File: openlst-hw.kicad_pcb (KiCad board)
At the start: 4 copper layers, 60 x 50 mm, 175 parts, among them J1 5VDC, J2 CC Prog/Debug, J3 UART0, J4 UART1, J5 Control Outputs, J6 ANT, U1 LM1117-3.3, U2 CC1110, U3 LT1086-3.6, U4 FOX924 27MHz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

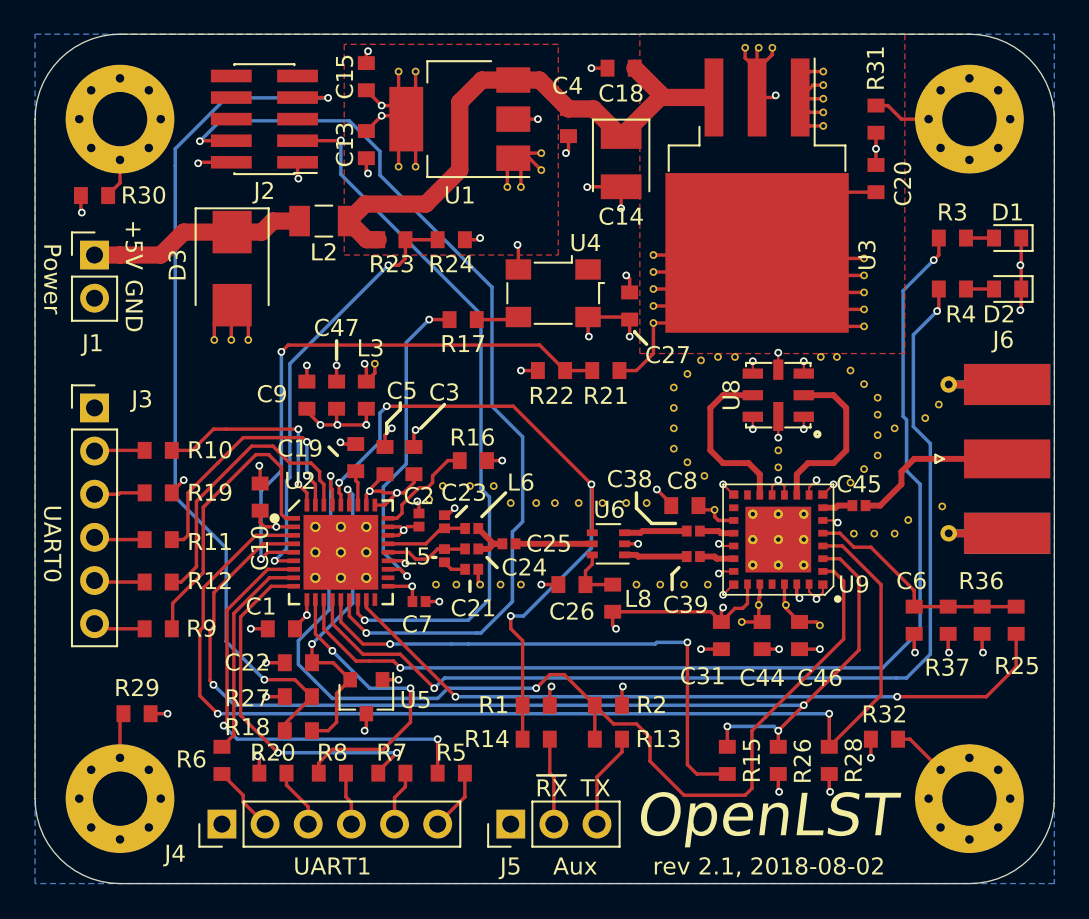
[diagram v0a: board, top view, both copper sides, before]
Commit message: Migrate to KiCad 7 files, schematic visual cleanup, pcb routing cleanup
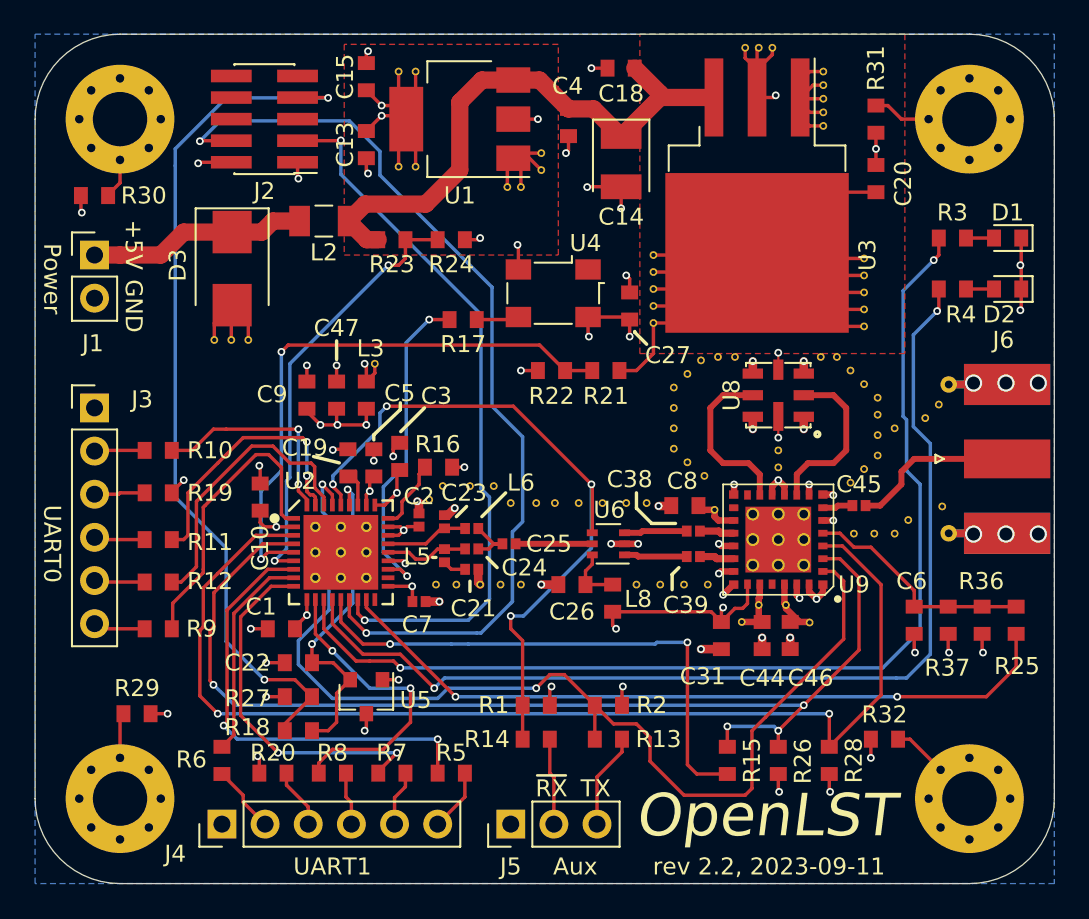
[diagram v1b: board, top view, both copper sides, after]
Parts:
- moved R16 2.09 mm to (137.2, 64.0)
- moved C3 0.87 mm to (135.0, 63.4)
- moved C5 0.67 mm to (133.4, 63.7)
- moved REF** 0.63 mm to (159.1, 73.1)
- moved C19 0.55 mm to (131.9, 63.7)
- moved C46 0.55 mm to (157.9, 73.9)
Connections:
- net /~LST_RESET renamed /~{LST_RESET}
- net /~LST_RX_MODE renamed /~{LST_RX_MODE}
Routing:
- net GND: track 94.4 -> 91.8 mm, vias 56 -> 63
- net /3V3_FILT: track 24.4 -> 22.0 mm
- net Net-(R16-Pad2): track 6.16 -> 4.21 mm
- net /LST_TX_MODE: track 63.9 -> 63.3 mm
- net VCC_3V6: track 105.7 -> 105.1 mm
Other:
- net class 50ohm removed
- net class 8mil removed
- net class Default removed
- net class PWR removed
- board text added: "rev 2.2, 2023-09-11"
- board text added: "rwk brb"
- board text added: "~{RX}"
- board text removed: "rev 2.1, 2018-08-02"
- board text removed: "rwk"
- board text removed: "~RX"

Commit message: DRC cleanup
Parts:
- moved C19 0.13 mm to (131.9, 63.6)
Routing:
- net /LST_TX_MODE: track 63.3 -> 64.5 mm

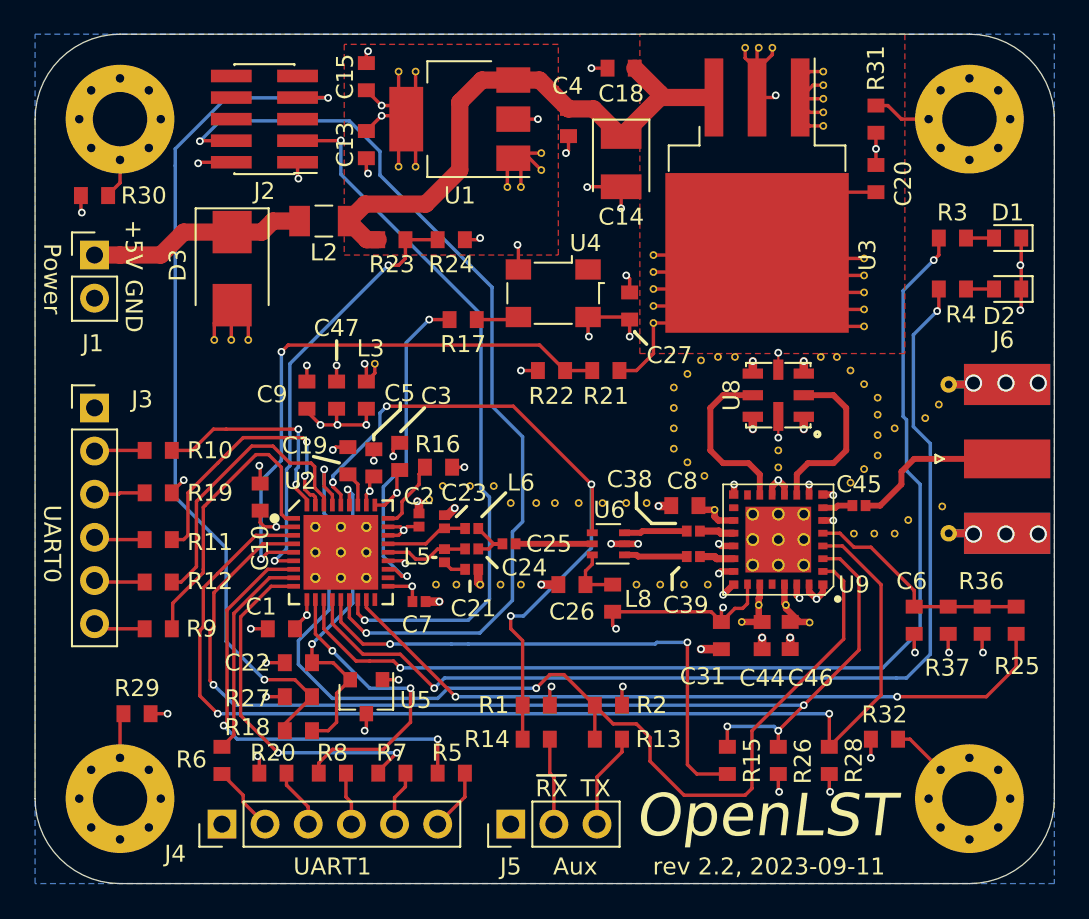
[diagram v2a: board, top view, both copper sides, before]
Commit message: Replace stitching pads with vias, add top ground fill
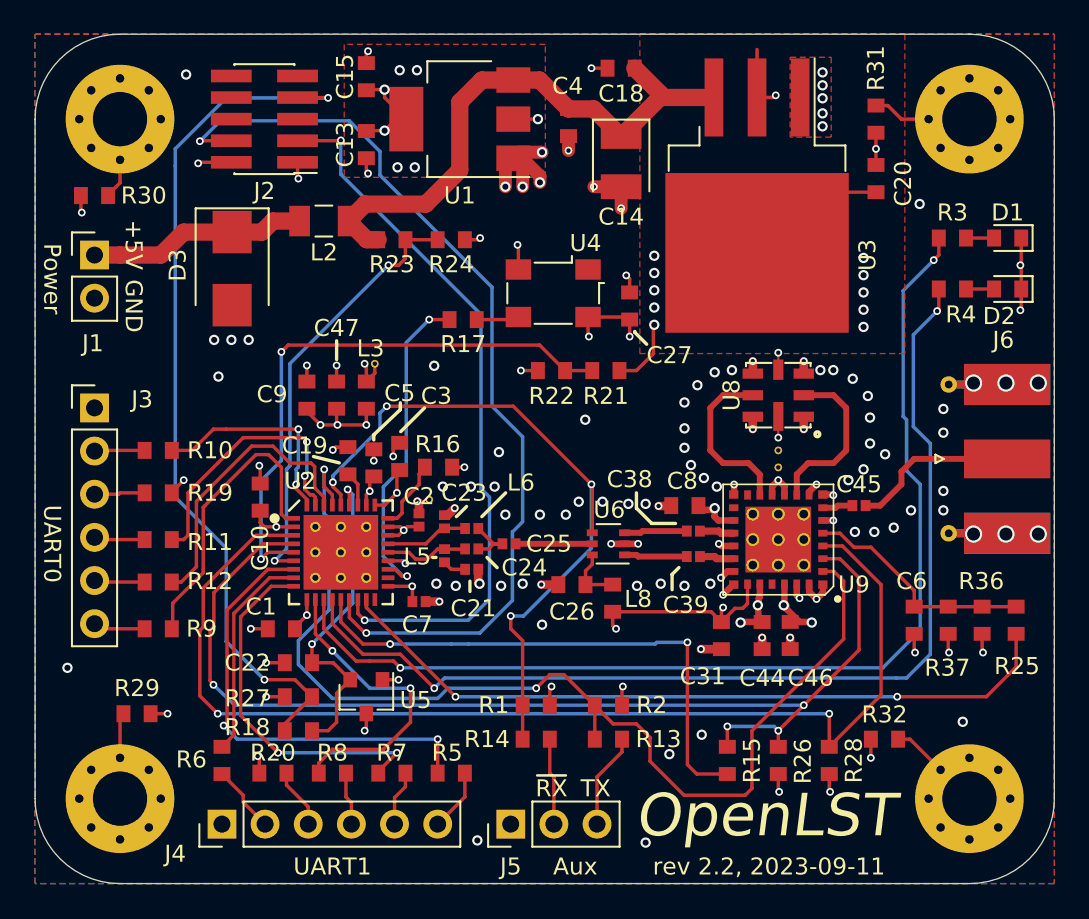
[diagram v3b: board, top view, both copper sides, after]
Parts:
- removed the REF** at (137.1, 70.9)
- removed the REF** at (153.7, 57.5)
- removed the REF** at (161.5, 64.9)
- removed the REF** at (163.1, 62.1)
- removed the REF** at (163.1, 60.9)
- removed the REF** at (163.1, 59.9)
- removed the REF** at (159.8, 57.5)
- removed the REF** at (164.1, 61.7)
- removed the REF** at (161.7, 67.9)
- removed the REF** at (162.9, 67.9)
- removed the REF** at (164.9, 67.1)
- removed the REF** at (166.9, 66.3)
- removed the REF** at (162.3, 64.1)
- removed the REF** at (160.7, 57.5)
- removed the REF** at (151.1, 59.3)
- removed the REF** at (149.5, 66.1)
- removed the REF** at (148.3, 66.1)
- removed the REF** at (146.9, 66.1)
- removed the REF** at (145.5, 66.1)
- removed the REF** at (144.1, 66.1)
- removed the REF** at (152.9, 64.5)
- removed the REF** at (143.0, 66.1)
- removed the REF** at (141.5, 66.1)
- removed the REF** at (140.5, 65.1)
- removed the REF** at (139.1, 65.1)
- removed the REF** at (137.5, 65.1)
- removed the REF** at (153.1, 70.9)
- removed the REF** at (151.7, 70.9)
- removed the REF** at (150.3, 70.9)
- removed the REF** at (148.9, 70.9)
- removed the REF** at (151.9, 63.7)
- removed the REF** at (142.1, 70.9)
- removed the REF** at (140.9, 70.9)
- removed the REF** at (139.7, 70.9)
- removed the REF** at (138.3, 70.9)
- removed the REF** at (151.1, 62.9)
- removed the REF** at (151.9, 58.5)
- removed the REF** at (154.7, 57.5)
- removed the REF** at (162.3, 59.1)
- removed the REF** at (163.1, 63.3)
- removed the REF** at (165.9, 61.1)
- removed the REF** at (151.1, 61.7)
- removed the REF** at (164.1, 67.9)
- removed the REF** at (162.3, 51.7)
- removed the REF** at (149.9, 51.5)
- removed the REF** at (162.3, 52.7)
- removed the REF** at (149.9, 52.5)
- removed the REF** at (162.3, 53.7)
- removed the REF** at (149.9, 53.5)
- removed the REF** at (162.3, 54.7)
- removed the REF** at (149.9, 54.5)
- removed the REF** at (162.3, 55.7)
- removed the REF** at (151.1, 60.5)
- removed the REF** at (149.9, 55.5)
- removed the REF** at (159.1, 73.1)
- removed the REF** at (155.1, 73.1)
- removed the REF** at (156.1, 72.1)
- removed the REF** at (157.7, 72.1)
- removed the REF** at (153.5, 66.5)
- removed the REF** at (156.9, 39.3)
- removed the REF** at (156.1, 39.3)
- removed the REF** at (155.3, 39.3)
- removed the REF** at (159.9, 41.5)
- removed the REF** at (161.5, 58.3)
- removed the REF** at (159.9, 42.3)
- removed the REF** at (159.9, 43.1)
- removed the REF** at (159.9, 43.9)
- removed the REF** at (159.9, 40.7)
- removed the REF** at (143.3, 45.5)
- removed the REF** at (143.3, 46.5)
- removed the REF** at (142.1, 47.5)
- removed the REF** at (141.3, 47.5)
- removed the REF** at (135.9, 40.7)
- removed the REF** at (134.9, 40.7)
- removed the REF** at (166.7, 60.3)
- removed the REF** at (135.9, 46.3)
- removed the REF** at (134.9, 46.3)
- removed the REF** at (126.0, 56.5)
- removed the REF** at (125.0, 56.5)
- removed the REF** at (124.0, 56.5)
- removed the REF** at (152.7, 57.7)
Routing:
- net VCC_3V6: track 105.1 -> 31.1 mm, vias 2 -> 17
- net GND: track 91.9 -> 74.7 mm, vias 63 -> 133
- net +3V3: track 46.5 -> 34.6 mm, vias 15 -> 19
- added copper zone on F.Cu, net GND
